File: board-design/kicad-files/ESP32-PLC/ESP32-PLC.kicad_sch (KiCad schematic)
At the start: 37 parts, among them J1 640456-3, J2 Conn_ARM_JTAG_SWD_10, J3 302-S101, J4 302-S101, Q1 BC817, Q2 BC817, U1 BD48ExxG, U2 ESP32-WROVER-E

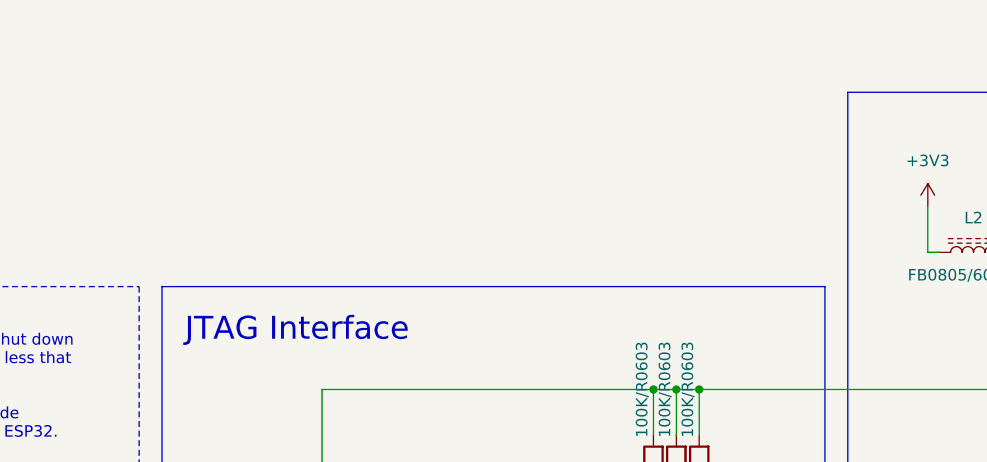
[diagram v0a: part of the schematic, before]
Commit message: [UPDATE]
Finished ESP32 and ESP32-programmer board designs (few corrections to be made when manufacturer is chosen - design rules).

Signed-off-by: Nicolae-Andrei Vasile <vasilenicolaeandrei@gmail.com>
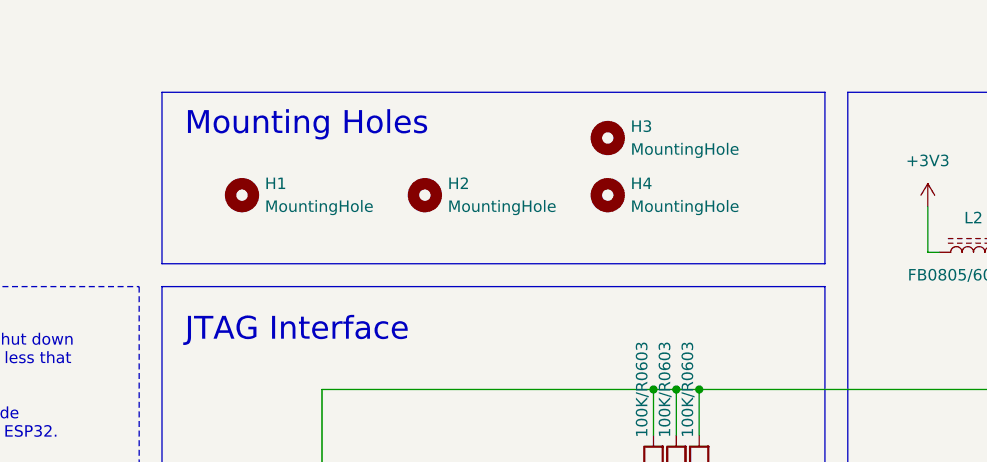
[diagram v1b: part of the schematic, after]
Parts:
- added H1, H2, H3, H4: MountingHole, MountingHole:MountingHole_2.5mm_Pad_Via, symbol Mechanical:MountingHole
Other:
- note added: "Mounting Holes"
- title: PLC -> ESP32
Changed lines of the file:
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@@
   (paper "A4")
   (title_block
-    (title "PLC")
-    (date "2023-08-20")
+    (title "ESP32")
+    (date "2023-12-03")
     (rev "A")
+    (comment 1 "Author: Nicolae-Andrei Vasile")
   )
   (junction (at 86.36 171.45) (diameter 0) (color 0 0 0 0)
@@
     (fill (type none))
   )
+  (rectangle (start 66.04 13.97) (end 139.7 33.02)
+    (stroke (width 0) (type default) (color 140 140 0 1))
+    (fill (type none))
+  )
   (text_box "Observations:\n\nVoltage supervisor added to safely shut down ESP32 when the power supply feeds less that 2.7V to the source pin.\n\nAuto-program (Boot & Enable) is made available via UART interface to flash ESP32.\n___________________________\nDTR		RTS	->	EN		IO0\n___________________________\n1		1		1		1\n0		0		1		1\n1		0		0		1\n0		1		1		0\n\nThe 0Ohm resistor may be removed in order to isolate the JTAG port from this system reset signal. Other 0Ohm resisteors are present for debug purposes.\n\nSPI interface and JTAG debug interface share the same 4 pins for communication. The hardware must be configured accordingly for each module to be accessed."
     (at 15.24 35.56 0) (size 48.26 66.04)
@@
   )
   (text "PWR References\n" (at 17.78 146.05 0)
+    (effects (font (size 2.54 2.54) (color 140 140 0 1)) (justify left bottom))
+  )
+  (text "Mounting Holes" (at 68.58 19.05 0)
     (effects (font (size 2.54 2.54) (color 140 140 0 1)) (justify left bottom))
   )
@@
     )
   )
+  (symbol (lib_id "Mechanical:MountingHole") (at 115.57 25.4 0) (unit 1)
+    (in_bom yes) (on_board yes) (dnp no) (fields_autoplaced)
+    (property "Reference" "H4" (at 118.11 24.13 0)
+      (effects (font (size 1.27 1.27)) (justify left))
+    )
+    (property "Value" "MountingHole" (at 118.11 26.67 0)
+      (effects (font (size 1.27 1.27)) (justify left))
+    )
+    (property "Footprint" "MountingHole:MountingHole_2.5mm_Pad_Via" (at 115.57 25.4 0)
+      (effects (font (size 1.27 1.27)) hide)
+    )
+    (property "Datasheet" "~" (at 115.57 25.4 0)
+      (effects (font (size 1.27 1.27)) hide)
+    )
+    (instances
+      (project "ESP32-PLC"
+        (path "/73e71d8b-00c7-414e-8d46-984de36f83d3"
+          (reference "H4") (unit 1)
+        )
+      )
+    )
+  )
   (symbol (lib_id "Device:R") (at 123.19 55.88 180) (unit 1)
     (in_bom yes) (on_board yes) (dnp no)
@@
     )
   )
+  (symbol (lib_id "Mechanical:MountingHole") (at 95.25 25.4 0) (unit 1)
+    (in_bom yes) (on_board yes) (dnp no) (fields_autoplaced)
+    (property "Reference" "H2" (at 97.79 24.13 0)
+      (effects (font (size 1.27 1.27)) (justify left))
+    )
+    (property "Value" "MountingHole" (at 97.79 26.67 0)
+      (effects (font (size 1.27 1.27)) (justify left))
+    )
+    (property "Footprint" "MountingHole:MountingHole_2.5mm_Pad_Via" (at 95.25 25.4 0)
+      (effects (font (size 1.27 1.27)) hide)
+    )
+    (property "Datasheet" "~" (at 95.25 25.4 0)
+      (effects (font (size 1.27 1.27)) hide)
+    )
+    (instances
+      (project "ESP32-PLC"
+        (path "/73e71d8b-00c7-414e-8d46-984de36f83d3"
+          (reference "H2") (unit 1)
+        )
+      )
+    )
+  )
   (symbol (lib_id "Device:C_Polarized") (at 191.77 38.1 0) (mirror y) (unit 1)
     (in_bom yes) (on_board yes) (dnp no)
@@
         (path "/73e71d8b-00c7-414e-8d46-984de36f83d3/153766c4-5539-4687-8dd8-c000826b4aca"
           (reference "#PWR08") (unit 1)
+        )
+      )
+    )
+  )
+  (symbol (lib_id "Mechanical:MountingHole") (at 115.57 19.05 0) (unit 1)
+    (in_bom yes) (on_board yes) (dnp no) (fields_autoplaced)
+    (property "Reference" "H3" (at 118.11 17.78 0)
+      (effects (font (size 1.27 1.27)) (justify left))
+    )
+    (property "Value" "MountingHole" (at 118.11 20.32 0)
+      (effects (font (size 1.27 1.27)) (justify left))
+    )
+    (property "Footprint" "MountingHole:MountingHole_2.5mm_Pad_Via" (at 115.57 19.05 0)
+      (effects (font (size 1.27 1.27)) hide)
+    )
+    (property "Datasheet" "~" (at 115.57 19.05 0)
+      (effects (font (size 1.27 1.27)) hide)
+    )
+    (instances
+      (project "ESP32-PLC"
+        (path "/73e71d8b-00c7-414e-8d46-984de36f83d3"
+          (reference "H3") (unit 1)
         )
       )
@@
         )
       )
+    )
+  )
+  (symbol (lib_id "Mechanical:MountingHole") (at 74.93 25.4 0) (unit 1)
+    (in_bom yes) (on_board yes) (dnp no) (fields_autoplaced)
+    (property "Reference" "H1" (at 77.47 24.13 0)
+      (effects (font (size 1.27 1.27)) (justify left))
+    )
+    (property "Value" "MountingHole" (at 77.47 26.67 0)
+      (effects (font (size 1.27 1.27)) (justify left))
+    )
+    (property "Footprint" "MountingHole:MountingHole_2.5mm_Pad_Via" (at 74.93 25.4 0)
+      (effects (font (size 1.27 1.27)) hide)
+    )
+    (property "Datasheet" "~" (at 74.93 25.4 0)
+      (effects (font (size 1.27 1.27)) hide)
+    )
+    (instances
+      (project "ESP32-PLC"
+        (path "/73e71d8b-00c7-414e-8d46-984de36f83d3"
+          (reference "H1") (unit 1)
+        )
+      )

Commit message: [FIX]
Updated footprints for tactile switches.

Signed-off-by: Nicolae-Andrei Vasile <vasilenicolaeandrei@gmail.com>
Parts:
- S1, S2: footprint Button_Switch_SMD:SW_MEC_5GSH9 -> digikey-footprints:Switch_Tactile_THT_6x6mm
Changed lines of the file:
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@@
       (effects (font (size 1.524 1.524)) (justify left))
     )
-    (property "Footprint" "Button_Switch_SMD:SW_MEC_5GSH9" (at 129.54 184.15 0)
+    (property "Footprint" "digikey-footprints:Switch_Tactile_THT_6x6mm" (at 129.54 184.15 0)
       (effects (font (size 1.524 1.524)) (justify left) hide)
     )
@@
       (effects (font (size 1.524 1.524)) (justify left))
     )
-    (property "Footprint" "Button_Switch_SMD:SW_MEC_5GSH9" (at 160.02 184.15 0)
-      (effects (font (size 1.524 1.524)) (justify left) hide)
-    )
+    (property "Footprint" "digikey-footprints:Switch_Tactile_THT_6x6mm" (at 160.02 184.15 0)
+      (effects (font (size 1.524 1.524)) (justify left) hide)
+    )

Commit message: [UPDATE]
Work in progress.

Signed-off-by: Nicolae-Andrei Vasile <vasilenicolaeandrei@gmail.com>
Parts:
- removed J4: 302-S101, Connector_IDC:IDC-Header_2x05_P2.54mm_Vertical, symbol dk_Rectangular-Connectors-Headers-Male-Pins:302-S101
- added J4: Conn_02x05_Odd_Even, Connector_IDC:IDC-Header_2x05_P2.54mm_Vertical, symbol Connector_Generic:Conn_02x05_Odd_Even
- added J5: Conn_02x10_Odd_Even, Connector_IDC:IDC-Header_2x10_P2.54mm_Vertical, symbol Connector_Generic:Conn_02x10_Odd_Even
- renumbered C5 to C3, C6 to C4, C7 to C5, C8 to C6, C3 to C7, C4 to C8, JP3 to JP2, JP5 to JP3, JP2 to JP5, R4 to R3, R5 to R4, R3 to R5
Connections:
- net +3V3: now also J4.1 (Pin_1), J4.2 (Pin_2), J5.19 (Pin_19), J5.20 (Pin_20)
- net CS0: now also R9.1; no longer R10.1
- net ESP32_INT: now also J4.5 (Pin_5)
- net GND: now also J4.7 (Pin_7), J4.9 (Pin_9), J5.16 (Pin_16), J5.18 (Pin_18)
- net MISO: now also R10.1; no longer R12.1
- net MOSI: now also R12.1; no longer R9.1
- net SAM4E_INT: now also J4.3 (Pin_3)
- net at R9.2: now also J4.4 (Pin_4)
- net at R10.2: now also J4.6 (Pin_6)
- net at R11.2: now also J4.8 (Pin_8)
- net at R12.2: now also J4.10 (Pin_10)
- new net LTE/LTE_AP_READY: J5.11 (Pin_11)
- new net LTE/LTE_PWRKEY: J5.15 (Pin_15)
- new net LTE/LTE_RESET_N: J5.17 (Pin_17)
- new net LTE/LTE_STATUS: J5.13 (Pin_13)
- new net LTE/LTE_UART_DBG_RXD: J5.5 (Pin_5)
- new net LTE/LTE_UART_DBG_TXD: J5.1 (Pin_1)
- new net LTE/LTE_UART_DTR: J5.3 (Pin_3)
- new net LTE_UART_CTS: J5.4 (Pin_4)
- new net LTE_UART_DCD: J5.2 (Pin_2)
- new net LTE_UART_RI: J5.6 (Pin_6)
- new net LTE_UART_RTS: J5.8 (Pin_8)
- new net LTE_UART_RXD: J5.10 (Pin_10)
- new net LTE_UART_TXD: J5.12 (Pin_12)
- new net RTC_EEPROM/RTC_MFP: J5.14 (Pin_14)
- new net RTC_EEPROM/SCL: J5.7 (Pin_7)
- new net RTC_EEPROM/SDA: J5.9 (Pin_9)
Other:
- added sheet LTE (LTE.kicad_sch)
- added sheet RTC_EEPROM (RTC_EEPROM.kicad_sch)
- note added: "UART&I2C Interface"
- moved on the sheet: C1, C2, C3, C4, C5, C6, C7, C8, H1, H2, H3, H4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

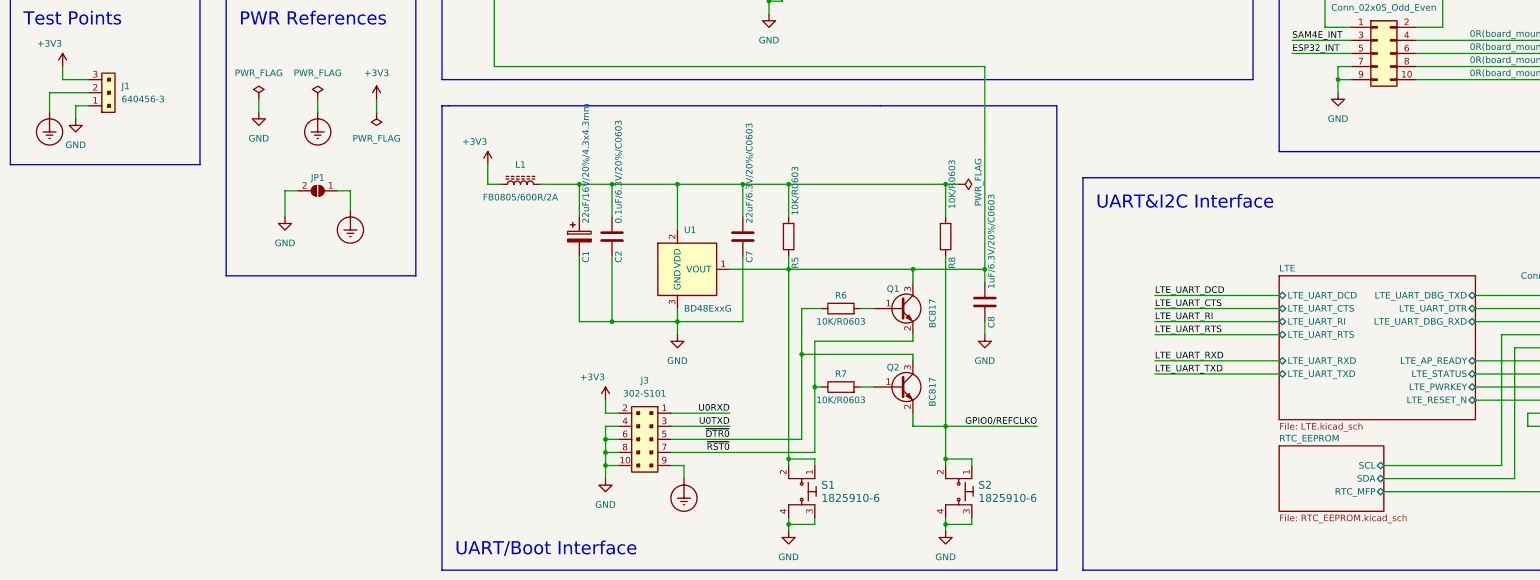
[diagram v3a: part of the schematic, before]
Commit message: [UPDATE]
Finished ESP32-PLC board design

Signed-off-by: Nicolae-Andrei Vasile <vasilenicolaeandrei@gmail.com>
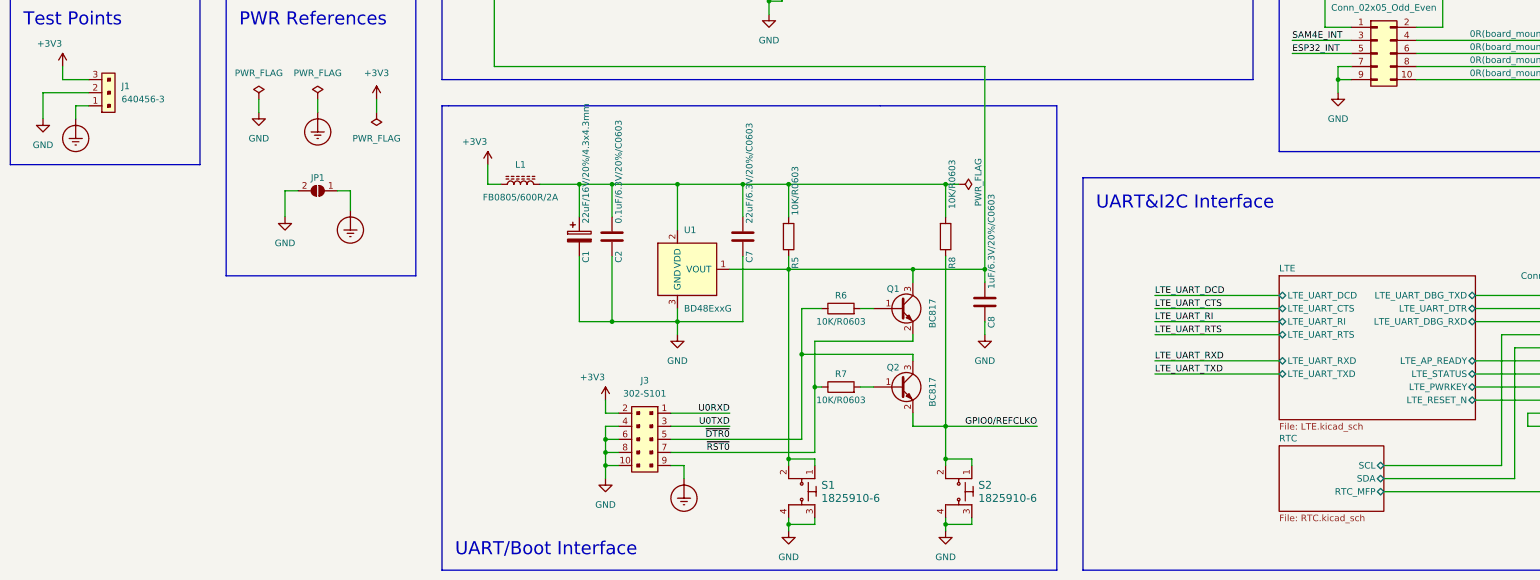
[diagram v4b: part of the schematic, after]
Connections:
- net Earth_Protective: now also J1.1; no longer J1.2
- net GND: now also J1.2; no longer J1.1
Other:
- sheet RTC_EEPROM renamed RTC
- sheet RTC: file RTC_EEPROM.kicad_sch -> RTC.kicad_sch
